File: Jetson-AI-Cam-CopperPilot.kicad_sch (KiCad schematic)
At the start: 0 parts

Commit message: feat: setup reference Jetson Nano baseboard, sanitize antmicro attribution, and normalize libraries
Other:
- added sheet CSI (csi.kicad_sch)
- added sheet Display (display.kicad_sch)
- added sheet ID Serial (id-serial.kicad_sch)
- added sheet Interfaces (interfaces.kicad_sch)
- added sheet SoM (som.kicad_sch)
- added sheet Supply (supply.kicad_sch)
- added sheet USB (usb-debug.kicad_sch)
- title: (none) -> Jetson Stereo AI Camera

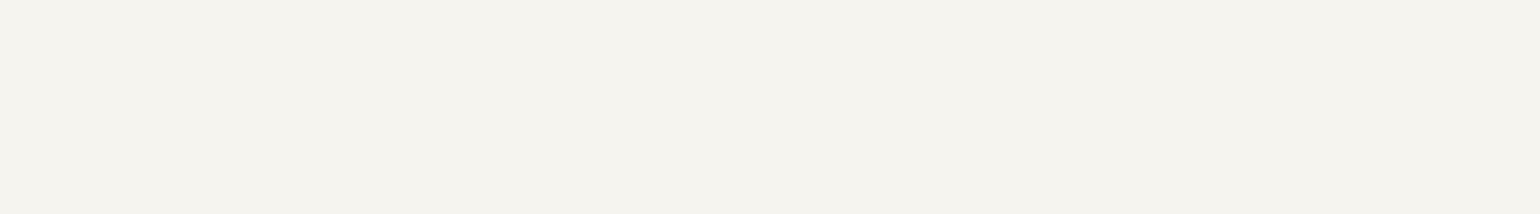
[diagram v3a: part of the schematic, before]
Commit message: feat(release): resolve all ERC/DRC/parity issues, complete 8-layer routing, and generate JLCPCB fab outputs
Resolve all schematic ERC violations, PCB DRC errors/warnings, schematic-to-PCB parity mismatches, and LCSC BOM/CPL fields, and package 8-layer Gerbers, drills, BOM, and CPL for JLCPCB manufacturing.

Co-Authored-By: CopperPilot <noreply@copperpilot.ai>
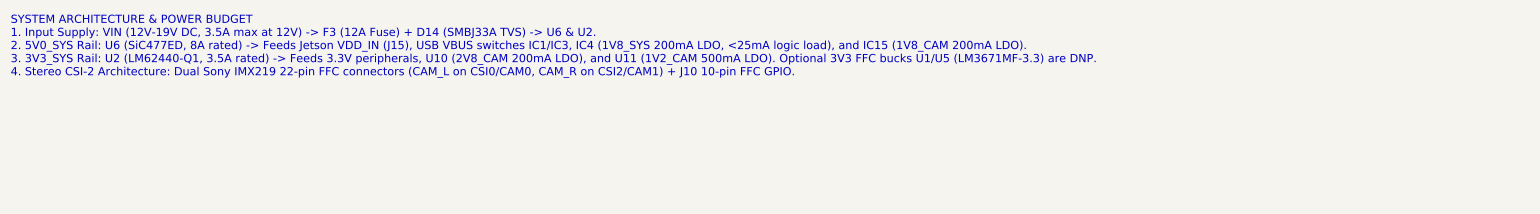
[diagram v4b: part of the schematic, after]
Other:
- note added: "SYSTEM ARCHITECTURE & POWER BUDGET 1. Input Supply: VIN (12V-19V DC, 3.5A max at 12V) -> F3 (12A Fuse) + D14 (SMBJ33A TVS) -> U6 & U2. 2. 5V0_SYS Rail: U6 (SiC477ED, 8A rated) -> Feeds Jetson VDD_IN (J15), USB VBUS switches IC1/IC3, IC4 (1V8_SYS 200mA LDO, <25mA logic load), and IC15 (1V8_CAM 200mA LDO). 3. 3V3_SYS Rail: U2 (LM62440-Q1, 3.5A rated) -> Feeds 3.3V peripherals, U10 (2V8_CAM 200mA LD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"
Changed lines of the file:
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@@
+		)
+	)
+	(text "SYSTEM ARCHITECTURE & POWER BUDGET\n1. Input Supply: VIN (12V-19V DC, 3.5A max at 12V) -> F3 (12A Fuse) + D14 (SMBJ33A TVS) -> U6 & U2.\n2. 5V0_SYS Rail: U6 (SiC477ED, 8A rated) -> Feeds Jetson VDD_IN (J15), USB VBUS switches IC1/IC3, IC4 (1V8_SYS 200mA LDO, <25mA logic load), and IC15 (1V8_CAM 200mA LDO).\n3. 3V3_SYS Rail: U2 (LM62440-Q1, 3.5A rated) -> Feeds 3.3V peripherals, U10 (2V8_CAM 200mA LDO), and U11 (1V2_CAM 500mA LDO). Optional 3V3 FFC bucks U1/U5 (LM3671MF-3.3) are DNP.\n4. Stereo CSI-2 Architecture: Dual Sony IMX219 22-pin FFC connectors (CAM_L on CSI0/CAM0, CAM_R on CSI2/CAM1) + J10 10-pin FFC GPIO."
+		(exclude_from_sim no)
+		(at 40.64 45.72 0)
+		(effects
+			(font
+				(size 1.524 1.524)
+			)
+			(justify left top)
 		)
 	)

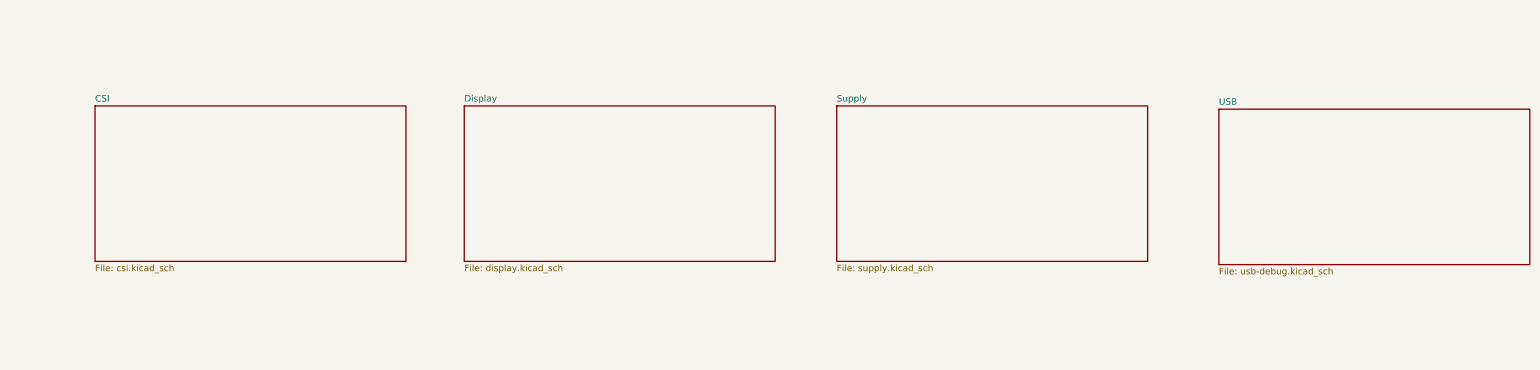
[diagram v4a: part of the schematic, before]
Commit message: fix(sch): resolve label, wire, and property collisions on Root, ID Serial, and Interfaces sheets
Remove duplicate overlapping global labels on GEN0_SDA, GEN0_SCL, and 3V3_SYS, delete off-sheet stray artifacts, reposition R71/R101/C13 properties out of wire corridors, clear J14 MP pin number from vertical GND drop, and align hierarchical sheets to 1.27mm grid.

Co-Authored-By: CopperPilot <noreply@copperpilot.ai>
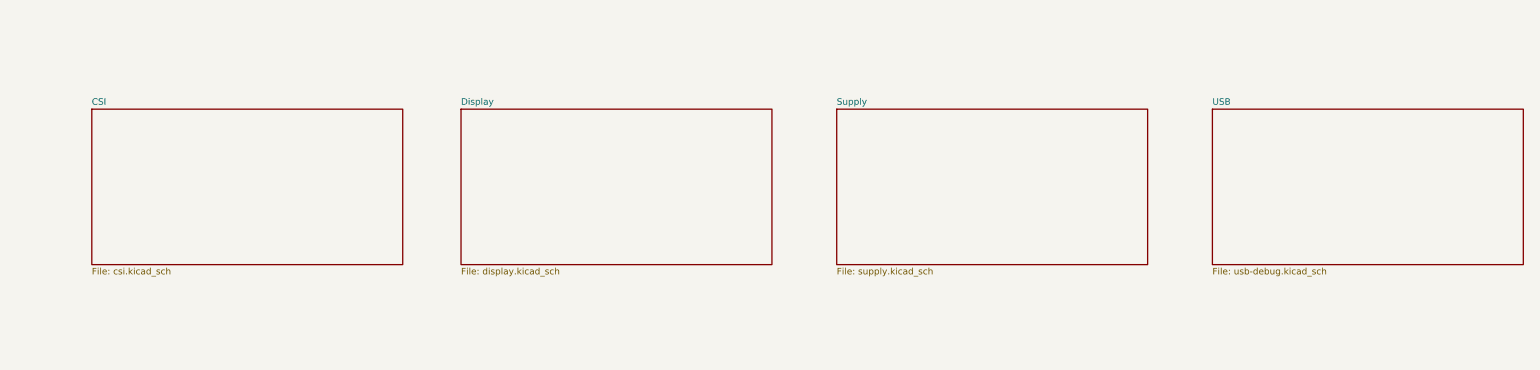
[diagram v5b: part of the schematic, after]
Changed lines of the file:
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@@
 	)
 	(sheet
-		(at 209.55 159.385)
+		(at 209.55 160.02)
 		(size 60.96 30.48)
 		(exclude_from_sim no)
@@
 		)
 		(property "Sheetname" "Supply"
-			(at 209.55 158.6734 0)
+			(at 209.55 159.3084 0)
 			(show_name no)
 			(do_not_autoplace no)
@@
 		)
 		(property "Sheetfile" "supply.kicad_sch"
-			(at 209.55 190.4496 0)
+			(at 209.55 191.0846 0)
 			(show_name no)
 			(do_not_autoplace no)
@@
 	)
 	(sheet
-		(at 284.48 160.02)
+		(at 283.21 160.02)
 		(size 60.96 30.48)
 		(exclude_from_sim no)
@@
 		)
 		(property "Sheetname" "USB"
-			(at 284.48 159.3084 0)
+			(at 283.21 159.3084 0)
 			(show_name no)
 			(do_not_autoplace no)
@@
 		)
 		(property "Sheetfile" "usb-debug.kicad_sch"
-			(at 284.48 191.0846 0)
+			(at 283.21 191.0846 0)
 			(show_name no)
 			(do_not_autoplace no)
@@
 	)
 	(sheet
-		(at 136.525 159.385)
+		(at 135.89 160.02)
 		(size 60.96 30.48)
 		(exclude_from_sim no)
@@
 		)
 		(property "Sheetname" "Display"
-			(at 136.525 158.6734 0)
+			(at 135.89 159.3084 0)
 			(show_name no)
 			(do_not_autoplace no)
@@
 		)
 		(property "Sheetfile" "display.kicad_sch"
-			(at 136.525 190.4496 0)
+			(at 135.89 191.0846 0)
 			(show_name no)
 			(do_not_autoplace no)
@@
 	)
 	(sheet
-		(at 64.135 159.385)
+		(at 63.5 160.02)
 		(size 60.96 30.48)
 		(exclude_from_sim no)
@@
 		)
 		(property "Sheetname" "CSI"
-			(at 64.135 158.6734 0)
+			(at 63.5 159.3084 0)
 			(show_name no)
 			(do_not_autoplace no)
@@
 		)
 		(property "Sheetfile" "csi.kicad_sch"
-			(at 64.135 190.4496 0)
-			(show_name no)
-			(do_not_autoplace no)
+			(at 63.5 191.0846 0)
+			(show_name no)
+			(do_not_autoplace no)
